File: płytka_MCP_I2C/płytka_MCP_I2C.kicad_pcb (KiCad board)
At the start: 2 copper layers, 80 x 77 mm, 37 parts, among them J1 A0, J10 V0, J11 Ext, J12 I2C, J13 U2, J15 U2, J16 U3, J17 RS, J18 K, J19 A, J2 A1, J20 VDD, J21 GND, J23 VSS, J24 Conn_01x16_Pin, J25 LCD, J26 VCC, J3 A2, J4 SDA, J5 SCL, J6 INTA, J7 INTB, J8 INTA, J9 RESET, U1 MCP23017_SP

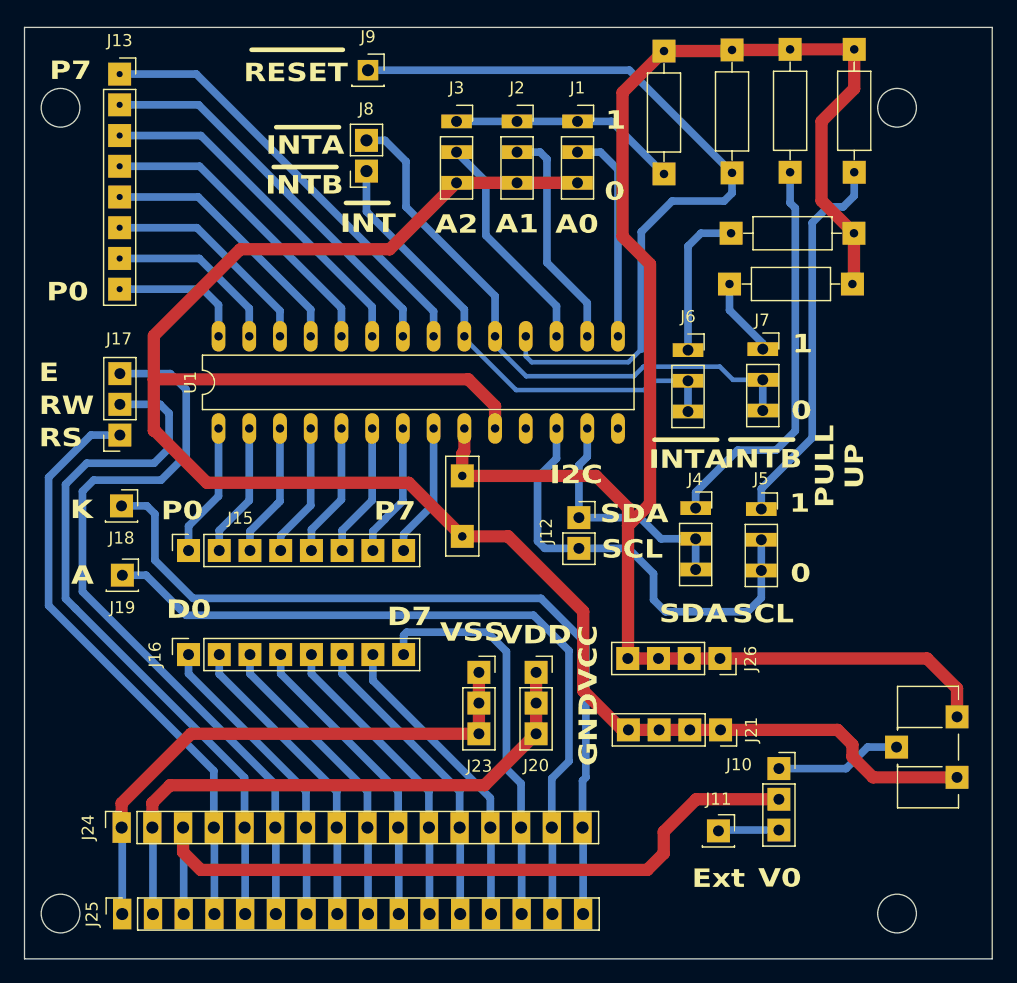
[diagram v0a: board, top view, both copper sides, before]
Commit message: Dodanie plytkek z wersja na frezowanie
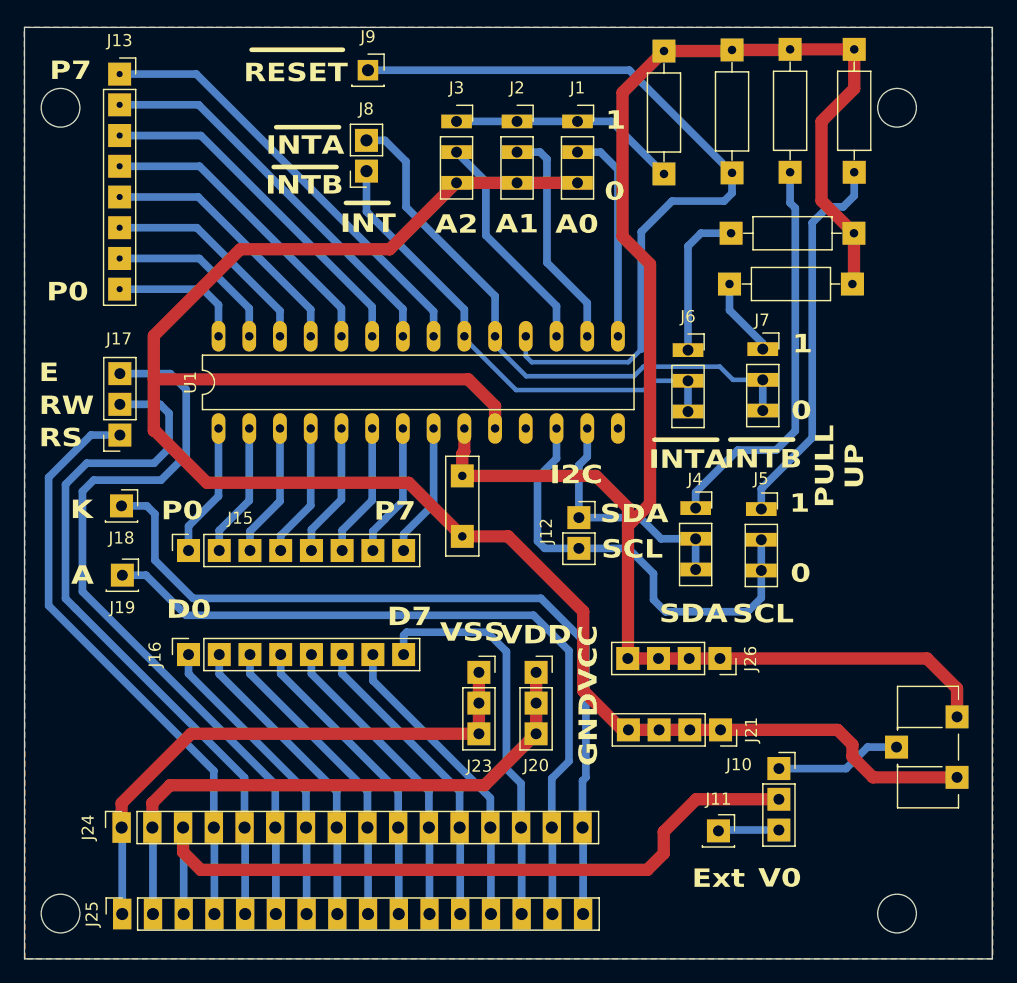
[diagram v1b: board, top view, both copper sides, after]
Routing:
- added copper zone on B.Cu, net GND
- added copper zone on F.Cu, net GND
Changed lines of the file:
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@@
 			(pinfunction "Pin_1")
 			(pintype "passive")
-			(clearance 0.00254)
+			(clearance 0)
 		)
 		(pad "2" thru_hole rect
@@
 			(pinfunction "Pin_2")
 			(pintype "passive")
-			(clearance 0.00254)
+			(clearance 0)
 		)
 		(pad "3" thru_hole rect
@@
 			(pinfunction "Pin_1")
 			(pintype "passive")
-			(clearance 0.00254)
+			(clearance 0)
 		)
 		(pad "2" thru_hole rect
@@
 			(pinfunction "Pin_2")
 			(pintype "passive")
-			(clearance 0.00254)
+			(clearance 0)
 		)
 		(pad "3" thru_hole rect
@@
 			(pinfunction "Pin_1")
 			(pintype "passive")
-			(clearance 0.0254)
+			(clearance 0)
 		)
 		(pad "2" thru_hole rect
@@
 			(pinfunction "Pin_2")
 			(pintype "passive")
-			(clearance 0.0254)
+			(clearance 0)
 		)
 		(pad "3" thru_hole rect
@@
 			(pinfunction "Pin_3")
 			(pintype "passive")
-			(clearance 0.0254)
+			(clearance 0)
 		)
 		(embedded_fonts no)
@@
 			(pinfunction "GPB0")
 			(pintype "bidirectional")
-			(clearance 0.0254)
+			(clearance 0)
 		)
 		(pad "2" thru_hole oval
@@
 			(pinfunction "GPB1")
 			(pintype "bidirectional")
-			(clearance 0.0254)
+			(clearance 0)
 		)
 		(pad "3" thru_hole oval
@@
 			(pinfunction "GPB2")
 			(pintype "bidirectional")
-			(clearance 0.0254)
+			(clearance 0)
 		)
 		(pad "4" thru_hole oval
@@
 			(pinfunction "GPB3")
 			(pintype "bidirectional")
-			(clearance 0.0254)
+			(clearance 0)
 		)
 		(pad "5" thru_hole oval
@@
 			(pinfunction "GPB4")
 			(pintype "bidirectional")
-			(clearance 0.0254)
+			(clearance 0)
 		)
 		(pad "6" thru_hole oval
@@
 			(pinfunction "GPB5")
 			(pintype "bidirectional")
-			(clearance 0.0254)
+			(clearance 0)
 		)
 		(pad "7" thru_hole oval
@@
 			(pinfunction "GPB6")
 			(pintype "bidirectional")
-			(clearance 0.0254)
+			(clearance 0)
 		)
 		(pad "8" thru_hole oval
@@
 			(pinfunction "GPB7")
 			(pintype "output")
-			(clearance 0.0254)
+			(clearance 0)
 		)
 		(pad "9" thru_hole oval
@@
 			(pinfunction "VDD")
 			(pintype "power_in")
-			(clearance 0.0254)
+			(clearance 0)
 		)
 		(pad "10" thru_hole oval
@@
 			(pinfunction "VSS")
 			(pintype "power_in")
-			(clearance 0.0254)
+			(clearance 0)
 		)
 		(pad "11" thru_hole oval
@@
 			(pinfunction "NC")
 			(pintype "no_connect")
-			(clearance 0.0254)
+			(clearance 0)
 		)
 		(pad "12" thru_hole oval
@@
 			(pinfunction "SCK")
 			(pintype "input")
-			(clearance 0.0254)
+			(clearance 0)
 		)
 		(pad "13" thru_hole oval
@@
 			(pinfunction "SDA")
 			(pintype "bidirectional")
-			(clearance 0.0254)
+			(clearance 0)
 		)
 		(pad "14" thru_hole oval
@@
 			(pinfunction "NC")
 			(pintype "no_connect")
-			(clearance 0.0254)
+			(clearance 0)
 		)
 		(pad "15" thru_hole oval
@@
 			(pinfunction "A0")
 			(pintype "input")
-			(clearance 0.0254)
+			(clearance 0)
 		)
 		(pad "16" thru_hole oval
@@
 			(pinfunction "A1")
 			(pintype "input")
-			(clearance 0.0254)
+			(clearance 0)
 		)
 		(pad "17" thru_hole oval
@@
 			(pinfunction "A2")
 			(pintype "input")
-			(clearance 0.0254)
+			(clearance 0)
 		)
 		(pad "18" thru_hole oval
@@
 			(pinfunction "~{RESET}")
 			(pintype "input")
-			(clearance 0.0254)
+			(clearance 0)
 		)
 		(pad "19" thru_hole oval
@@
 			(pinfunction "INTB")
 			(pintype "tri_state")
-			(clearance 0.0254)
+			(clearance 0)
 		)
 		(pad "20" thru_hole oval
@@
 			(pinfunction "INTA")
 			(pintype "tri_state")
-			(clearance 0.0254)
+			(clearance 0)
 		)
 		(pad "21" thru_hole oval
@@
 			(pinfunction "GPA0")
 			(pintype "bidirectional")
-			(clearance 0.0254)
+			(clearance 0)
 		)
 		(pad "22" thru_hole oval
@@
 			(pinfunction "GPA1")
 			(pintype "bidirectional")
-			(clearance 0.0254)
+			(clearance 0)
 		)
 		(pad "23" thru_hole oval
@@
 			(pinfunction "GPA2")
 			(pintype "bidirectional")
-			(clearance 0.0254)
+			(clearance 0)
 		)
 		(pad "24" thru_hole oval
@@
 			(pinfunction "GPA3")
 			(pintype "bidirectional")
-			(clearance 0.0254)
+			(clearance 0)
 		)
 		(pad "25" thru_hole oval
@@
 			(pinfunction "GPA4")
 			(pintype "bidirectional")
-			(clearance 0.0254)
+			(clearance 0)
 		)
 		(pad "26" thru_hole oval
@@
 			(pinfunction "GPA5")
 			(pintype "bidirectional")
-			(clearance 0.0254)
+			(clearance 0)
 		)
 		(pad "27" thru_hole oval
@@
 			(pinfunction "GPA6")
 			(pintype "bidirectional")
-			(clearance 0.0254)
+			(clearance 0)
 		)
 		(pad "28" thru_hole oval
@@
 			(pinfunction "GPA7")
 			(pintype "output")
-			(clearance 0.0254)
+			(clearance 0)
 		)
 		(embedded_fonts no)
@@
 			(pinfunction "Pin_1")
 			(pintype "passive")
-			(clearance 0.00254)
+			(clearance 0)
 		)
 		(pad "2" thru_hole rect
@@
 			(pinfunction "Pin_2")
 			(pintype "passive")
-			(clearance 0.00254)
+			(clearance 0)
 		)
 		(pad "3" thru_hole rect
@@
 			(pinfunction "Pin_7")
 			(pintype "passive")
-			(clearance 0.1)
+			(clearance 0)
 		)
 		(pad "8" thru_hole rect
@@
 			(pinfunction "Pin_8")
 			(pintype "passive")
-			(clearance 0.1)
+			(clearance 0)
 		)
 		(embedded_fonts no)
@@
 		(net 51)
 	)
+	(zone
+		(net 18)
+		(net_name "GND")
+		(layers "F.Cu" "B.Cu")
+		(hatch edge 0.5)
+		(connect_pads
+			(clearance 1)
+		)
+		(min_thickness 0.25)
+		(filled_areas_thickness no)
+		(fill yes
+			(thermal_gap 0.5)
+			(thermal_bridge_width 0.5)
+		)
+		(polygon
+			(pts
+				(xy 53.5 38.35) (xy 133.525 38.35) (xy 133.55 115.35) (xy 53.55 115.35)
+			)
+		)
+	)
 	(group ""
